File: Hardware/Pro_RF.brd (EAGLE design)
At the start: 40.6 x 27.9 mm, 102 parts, among them U1 MCP73831, U2 915MHz, U5 ATmega32U4, U6 3.3V, Y2 8MHz

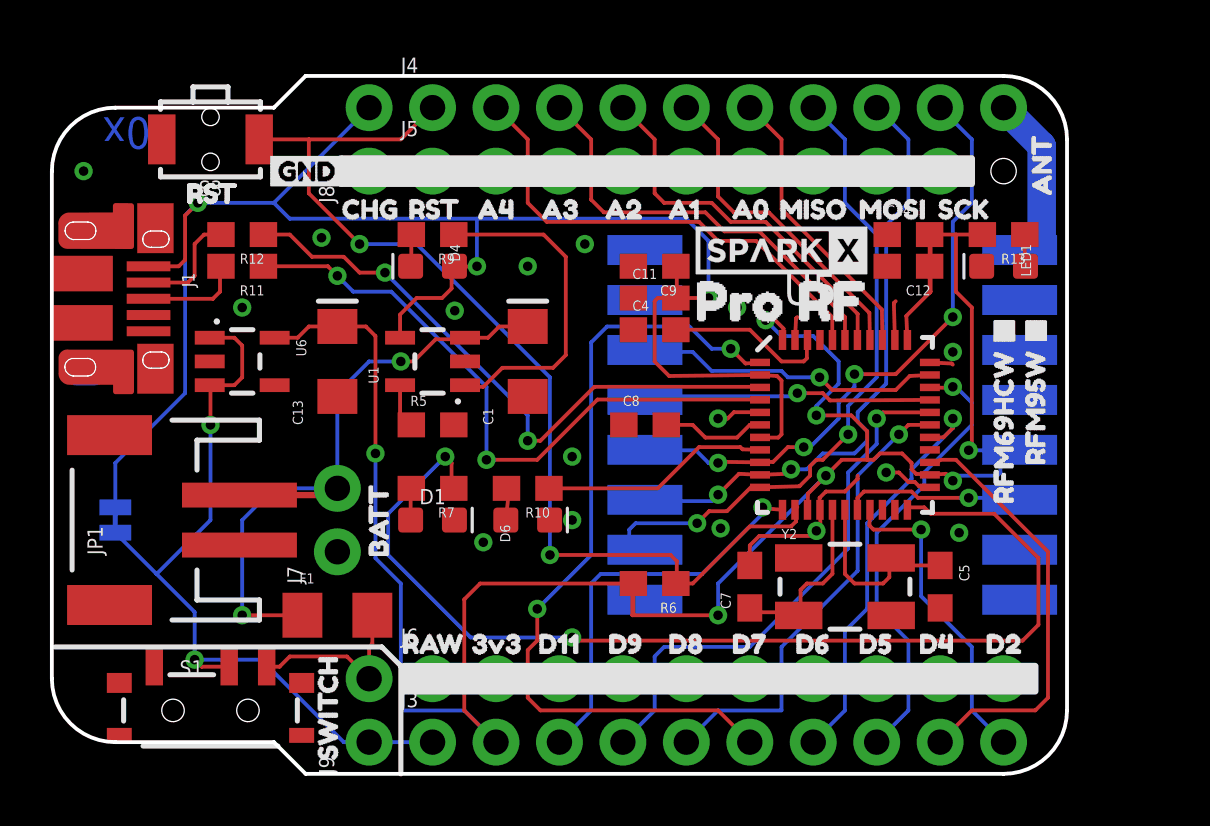
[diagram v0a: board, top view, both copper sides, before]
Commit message: Adding prod IDs. This changed some FPs so fixed routes. Moved Int Pin to avoid I2C
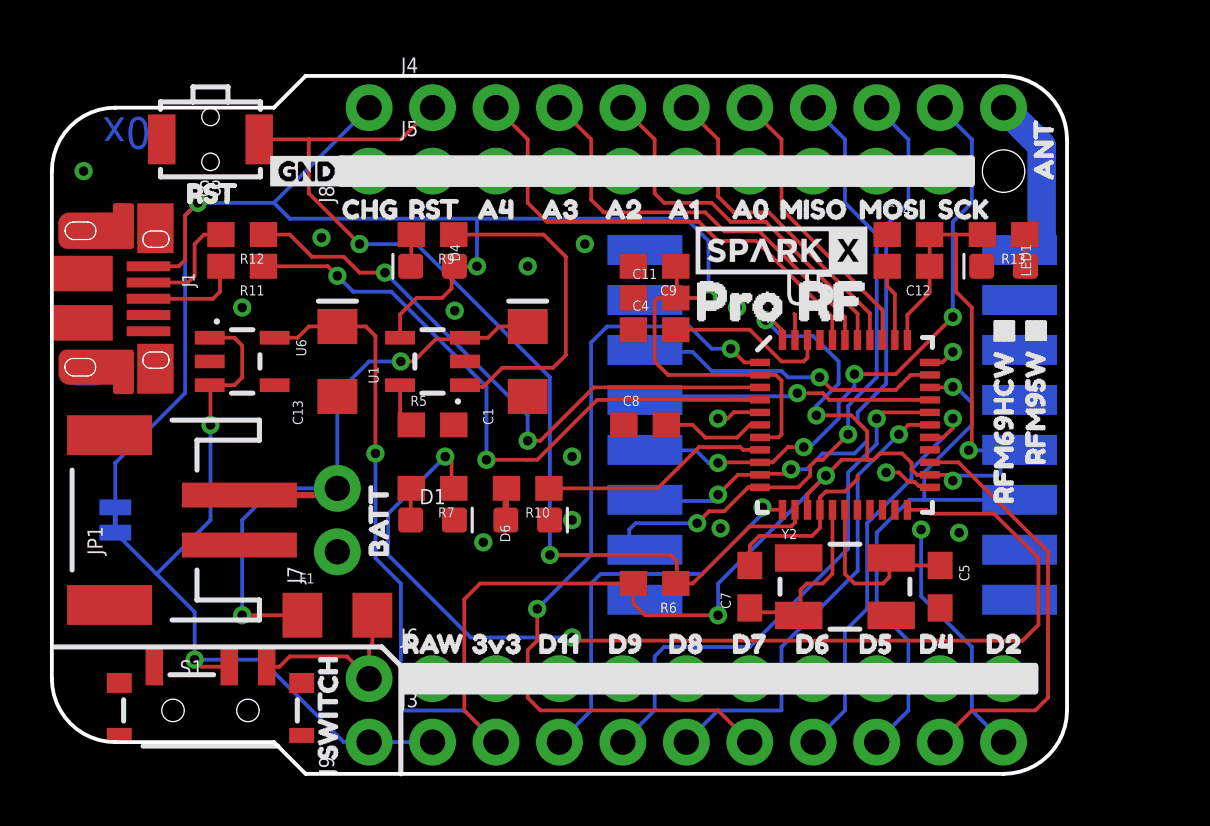
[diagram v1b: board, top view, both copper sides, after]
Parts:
- R10, R13, R7, R9: value 330 -> 1k
- S1: value (none) -> Power
- moved U$11 0.63 mm to (39.7, 23.1)
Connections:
- removed net D3: U2.14, U5.18
- removed net D5: J3.8, U5.31
- new net RFM_INT: J3.8, U2.14, U5.31
- new net SCL: U5.18
- new net SDA: U5.19
- net D2: no longer U5.19
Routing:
- net RFM_INT: track 0.00 -> 22.4 mm, vias 0 -> 1
- net D5: track 18.2 -> 0.00 mm, vias 1 -> 0
- net D3: track 7.21 -> 0.00 mm, vias 1 -> 0
- net 3.3V: track 92.5 -> 88.5 mm
- net D2: track 12.6 -> 9.88 mm
- net GND: track 14.6 -> 16.3 mm, vias 16 -> 15

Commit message: Many updates. v02.
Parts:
- removed U$61: (no value), buzzard_labels (25):D212
- removed U5: ATmega32U4, SparkFun-IC-Microcontroller:QFN-44-NOPAD
- added D2: BLUE, SparkFun-LED:LED-0603
- added J10: AVR_SPI_PROG_3X2TESTPOINTS, SparkFun-Connectors:2X3_TEST_POINTS
- added J11: (no value), SparkFun-Connectors:1X09_NO_SILK
- added J12: JST, SparkFun-Connectors:JST-2-SMD
- added J2: (no value), SparkFun-Connectors:1X04_1MM_RA
- added JP2: (no value), SparkFun-Jumpers:SMT-JUMPER_2_NO_SILK
- added R1, R2: 10k, SparkFun-Resistors:0603
- added R3: 1k, SparkFun-Resistors:0603
- added U$62: (no value), buzzard_labels (25):GND0
- added U$63: (no value), Labels:PWR-()-03
- added U$65: (no value), buzzard_labels (9):CHG1
- added U$66: (no value), Labels:QWIIC-()-04
- added U$68: (no value), buzzard_labels (9):D100
- added U$69: (no value), buzzard_labels (8):TX3
- added U$70: (no value), buzzard_labels (8):TX6
- added U$71: (no value), buzzard_labels (8):STAT5
- added U$72: (no value), buzzard_labels (8):RX7
- added U$73: (no value), buzzard_labels (8):RX2
- added U$74: (no value), buzzard_labels (25):D514
- added U3: 32U4, SparkFun-IC-Microcontroller:QFN-44-NOPAD
- D1: value GREEN -> Green
- D6: value BLUE -> Yellow
- J4: device SparkFun-Connectors:1X10_NO_SILK -> SparkFun-Connectors:1X01_NO_SILK
- J7: value (none) -> PTH
- J9: value (none) -> External On/Off
- JP1: device SparkFun-Connectors:JST-2-SMD -> SparkFun-Jumpers:SMT-JUMPER_2_NO_SILK
- SJ2: device SparkFun:SJ_2S-TRACE -> SparkFun-Jumpers:SMT-JUMPER_2_NC_TRACE_SILK
- U$15: device buzzard_labels (25):D212 -> buzzard_labels (10):D90
- U$16: device buzzard_labels (25):D413 -> buzzard_labels (10):D90
- U$17: device buzzard_labels (25):D514 -> buzzard_labels (25):GND0
- U$19: device buzzard_labels (25):D716 -> buzzard_labels (8):RX2
- U$21: device buzzard_labels (25):D918 -> buzzard_labels (9):D100
- U$25: device buzzard_labels (26):RFM69HCW_#0 -> buzzard_labels (3):LORA0
- U$26: value (none) -> SPECIAL_INSTRUCTIONS-ORDERING; device buzzard_labels (26):RFM95W_#1 -> SparkFun-Aesthetics:ORDERING_INSTRUCTIONS
- U$35: device buzzard_labels (25):RST2 -> buzzard_labels (3):WAN1
- U$55: device buzzard_labels (25):D918 -> buzzard_labels (25):D514
- U$57: device buzzard_labels (25):D716 -> buzzard_labels (8):TX3
- U$59: device buzzard_labels (25):D514 -> buzzard_labels (12):RFM69HCW#1
- U$60: device buzzard_labels (25):D413 -> buzzard_labels (12):RFM95W#0
- moved U$26 78.0 mm to (-34.3, -14.0), turned to 0 degrees
- moved R13 26.7 mm to (11.4, 21.1)
- moved J4 23.0 mm to (38.1, 24.1)
- moved U$25 22.3 mm to (15.9, 11.7), flipped to the bottom, turned to 270 degrees
- moved U$60 19.4 mm to (19.7, 13.7)
- moved LED1 19.1 mm to (19.1, 21.1), turned to 0 degrees
- moved C14 18.1 mm to (22.9, 7.62), turned to 90 degrees
- moved U$35 17.0 mm to (17.1, 11.7), flipped to the bottom, turned to 270 degrees
- moved U$59 16.0 mm to (22.2, 15.5)
- moved JP1 15.2 mm to (19.1, 10.2), flipped to the bottom, turned to 180 degrees
- moved U$51 15.2 mm to (2.54, 24.1)
- moved U$1 14.1 mm to (32.3, 7.24)
- moved U$19 13.1 mm to (39.6, 5.21), flipped to the bottom
- moved R6 12.8 mm to (25.4, 20.3), turned to 270 degrees
- moved U$15 12.7 mm to (24.0, 5.21)
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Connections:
- removed net A5: U5.41
- removed net D14: R10.1, U5.8
- removed net D2: J3.10
- removed net D4: J3.9, U5.25
- removed net D7: J3.6, U5.1
- removed net N$15: D1.A, R7.2
- removed net N$19: D6.A, R10.2
- removed net RST: J4.1, R6.1, S3.1, U5.13
- new net !CS: U2.5, U3.41
- new net !RST: J10.5, J11.1, R6.1, S3.1, U3.13
- new net D5: J3.8, U3.31
- new net N$1: D6.C, R10.2
- new net N$2: D1.C, R7.2
- new net N$3: D2.A, R3.1
- new net RFM_IO1: JP1.1, U2.15
- new net RFM_IO2: JP2.1, U2.16
- new net RXLED: R10.1, U3.8
- new net SHLD: J1.SHIELD, J1.SHIELD10, J1.SHIELD2, J1.SHIELD3, J1.SHIELD4, J1.SHIELD5, J1.SHIELD6, J1.SHIELD7, J1.SHIELD8, J1.SHIELD9
- new net STAT: R3.2, U3.32
- net 3.3V: now also D1.A, D6.A, J10.2, J2.2, U3.14, U3.24, U3.34, U3.44; no longer U5.14, U5.24, U5.34, U5.44
- net A0: now also J11.6, U3.36; no longer J4.6, U5.36
- net A1: now also J11.5, U3.37; no longer J4.5, U5.37
- net A2: now also J11.4, U3.38; no longer J4.4, U5.38
- net A3: now also J11.3, U3.39; no longer J4.3, U5.39
- net A4: now also J11.2, U3.40; no longer J4.2, U5.40
- net ANT: now also J4.1; no longer J4.10
- net AREF: now also U3.42; no longer U5.42
- net D+: now also U3.4; no longer U5.4
- net D-: now also U3.3; no longer U5.3
- net D10: now also J3.4, JP1.2, U3.30; no longer U2.5, U5.30
- net D11: now also JP2.2, U3.12; no longer U5.12
- net D6: now also U3.27; no longer U5.27
- net D8: now also J3.6, U3.28; no longer J3.5, U5.28
- net D9: now also J3.5, U3.29; no longer J3.4, U5.29
- net GND: now also D2.C, J10.6, J12.1, J2.1, R2.1, U3.15, U3.23, U3.33, U3.35, U3.43, U3.5; no longer D1.C, D6.C, JP1.1, U5.15, U5.23, U5.33, U5.35, U5.43, U5.5
- net MISO: now also J10.1, J11.7, U3.11; no longer J4.7, U5.11
- net MOSI: now also J10.4, J11.8, U3.10; no longer J4.8, U5.10
- net N$16: now also U3.16; no longer U5.16
- net N$17: now also U3.17; no longer U5.17
- net RFM_INT: now also U3.1; no longer J3.8, U5.31
- net RFM_RST: now also U3.25; no longer U5.32
- net RXI: now also J3.10, U3.20; no longer U5.20
- net SCK: now also J10.3, J11.9, U3.9; no longer J4.9, U5.9
- net SCL: now also J2.4, U3.18; no longer U5.18
- net SDA: now also J2.3, U3.19; no longer U5.19
- net TXLED: now also U3.22; no longer U5.22
- net TXO: now also J3.9, U3.21; no longer U5.21
- net UCAP: now also U3.6; no longer U5.6
- net USB_VCC: now also U3.2, U3.7; no longer U5.2, U5.7
- net VBATT: now also J12.2, R1.2; no longer JP1.2
- net VBATT_LVL: now also R1.1, R2.2, U3.26; no longer U5.26
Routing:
- net RST: track 41.8 -> 0.00 mm, vias 2 -> 0
- net VBATT_LVL: track 0.00 -> 37.8 mm, vias 0 -> 4
- net !RST: track 0.00 -> 36.1 mm, vias 0 -> 1
- net RFM_IO1: track 0.00 -> 35.4 mm, vias 0 -> 2
- net D10: track 11.6 -> 44.6 mm, vias 1 -> 4
- net D7: track 32.5 -> 0.00 mm, vias 2 -> 0
- net RFM_IO2: track 0.00 -> 27.7 mm
- net TXLED: track 42.7 -> 15.5 mm
- net RFM_RST: track 12.3 -> 34.1 mm, vias 1 -> 3
- net D5: track 0.00 -> 19.7 mm, vias 0 -> 1
- net D4: track 17.1 -> 0.00 mm
- net SCL: track 0.00 -> 13.1 mm, vias 0 -> 2
- net 3.3V: track 88.5 -> 101.4 mm, vias 7 -> 8
- net SDA: track 0.00 -> 12.0 mm, vias 0 -> 2
- net RXI: track 0.00 -> 11.8 mm, vias 0 -> 1
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- added copper zone on layer 1, net SHLD
- added copper zone on layer 16, net SHLD
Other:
- board text added: "+"
- board text added: "-"
- board text added: "0.8mm Board Thickness"
- board text added: "x02"
- board text removed: "x01"

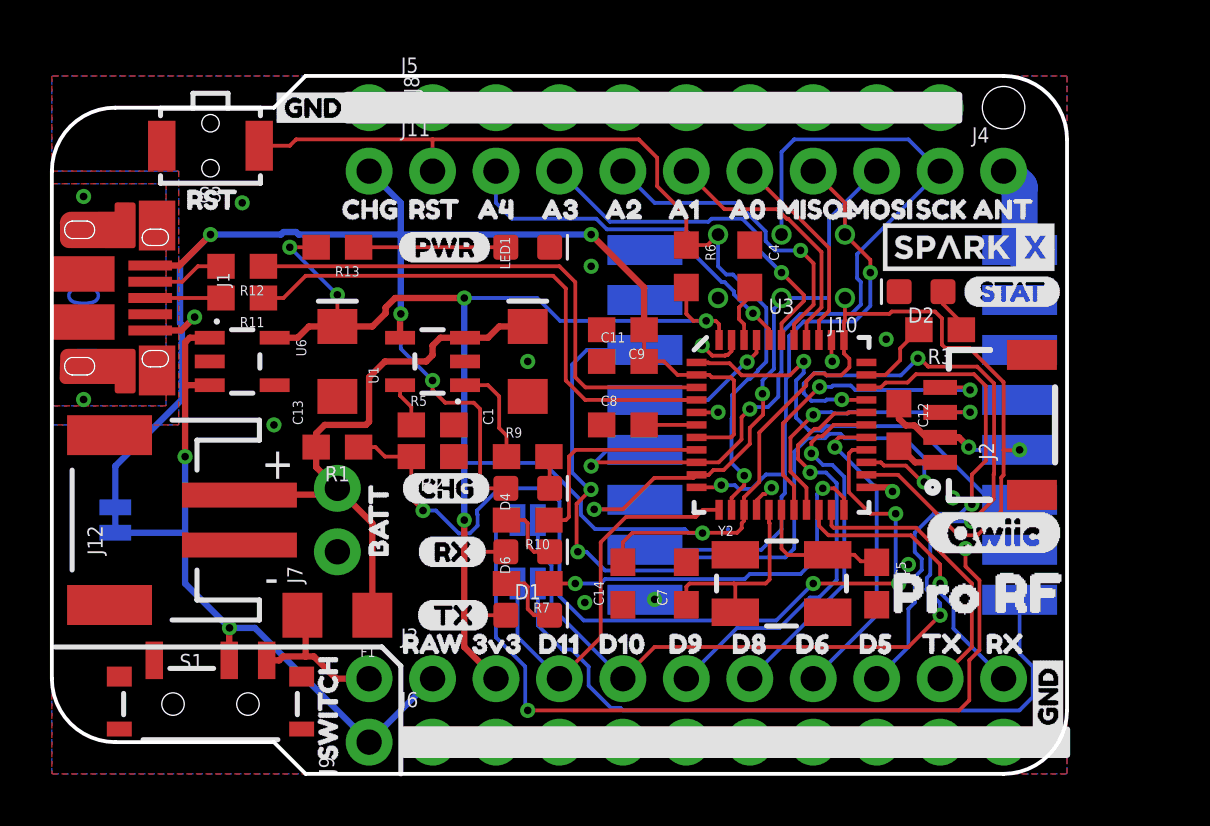
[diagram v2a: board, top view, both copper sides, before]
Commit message: Adding pullup to CS
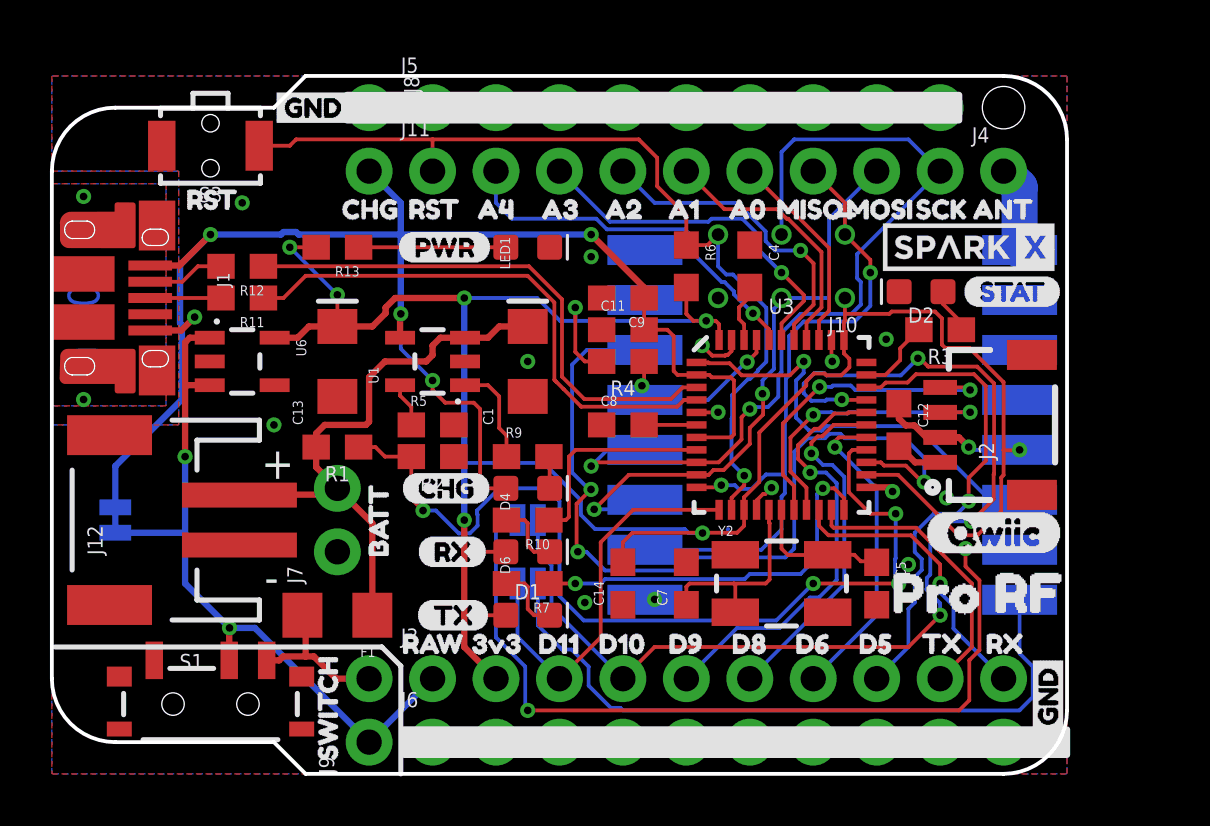
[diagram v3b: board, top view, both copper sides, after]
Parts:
- added R4: 10k, SparkFun-Resistors:0603
- moved C11 1.27 mm to (22.9, 17.8)
- moved C9 1.27 mm to (22.9, 19.1)
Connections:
- net !CS: now also R4.1
- net 3.3V: now also R4.2
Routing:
- net 3.3V: track 101.4 -> 104.9 mm, vias 8 -> 9
- net !CS: track 5.76 -> 7.39 mm, vias 1 -> 2

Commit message: Adding Examples
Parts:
- added FD1, FD2, FD3, FD4: FIDUCIAL1X2, SparkFun-Aesthetics:FIDUCIAL-1X2
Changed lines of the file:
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@@
 <attribute name="PROD_ID" value="RES-00824" x="22.86" y="16.51" size="1.778" layer="27" font="vector" ratio="15" rot="R180" display="off"/>
 </element>
+<element name="FD1" library="SparkFun-Aesthetics" package="FIDUCIAL-1X2" value="FIDUCIAL1X2" x="1.27" y="2.54" rot="MR0"/>
+<element name="FD2" library="SparkFun-Aesthetics" package="FIDUCIAL-1X2" value="FIDUCIAL1X2" x="39.37" y="25.4" rot="MR0"/>
+<element name="FD3" library="SparkFun-Aesthetics" package="FIDUCIAL-1X2" value="FIDUCIAL1X2" x="1.27" y="2.54"/>
+<element name="FD4" library="SparkFun-Aesthetics" package="FIDUCIAL-1X2" value="FIDUCIAL1X2" x="39.37" y="25.4"/>
 </elements>
 <signals>
@@
 <wire x1="25.03565625" y1="14.6986" x2="25.30705625" y2="14.97" width="0.1524" layer="1"/>
 <wire x1="21.19234375" y1="14.6986" x2="25.03565625" y2="14.6986" width="0.1524" layer="1"/>
-<wire x1="21.19234375" y1="14.6986" x2="20.485471875" y2="15.405471875" width="0.1524" layer="1"/>
-<wire x1="20.485471875" y1="15.405471875" x2="20.193" y2="15.69794375" width="0.1524" layer="1"/>
+<wire x1="21.19234375" y1="14.6986" x2="20.1168" y2="15.77414375" width="0.1524" layer="1"/>
 <wire x1="20.1168" y1="18.8722" x2="19.05" y2="19.939" width="0.1524" layer="1"/>
-<wire x1="20.193" y1="15.69794375" x2="20.1168" y2="15.77414375" width="0.1524" layer="1"/>
 <wire x1="20.1168" y1="15.77414375" x2="20.1168" y2="18.8722" width="0.1524" layer="1"/>
 </signal>
@@
 <wire x1="31.75" y1="18.1356" x2="31.71" y2="18.0956" width="0.1524" layer="1"/>
 <wire x1="33.528" y1="18.415" x2="31.75" y2="18.415" width="0.1524" layer="1"/>
-<wire x1="33.877" y1="11.97" x2="35.6235" y2="10.2235" width="0.1524" layer="1"/>
-<wire x1="35.6235" y1="10.2235" x2="36.2966" y2="9.5504" width="0.1524" layer="1"/>
+<wire x1="33.877" y1="11.97" x2="36.2966" y2="9.5504" width="0.1524" layer="1"/>
 <wire x1="30.51305625" y1="16.0274" x2="30.2006" y2="15.71494375" width="0.1524" layer="1"/>
 <wire x1="30.2006" y1="15.71494375" x2="30.2006" y2="15.54554375" width="0.1524" layer="1"/>

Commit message: updating to sparkfun silk
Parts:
- removed U$2, U$30: (no value), SparkX:SPARKX-SMALL
- added LOGO1: REVISION, SparkFun-Aesthetics:REVISION
- added LOGO2: SFE_LOGO_NAME.1_INCH, SparkFun-Aesthetics:SFE_LOGO_NAME_.1
- added LOGO3: SFE_LOGO_NAME_FLAME.1_INCH, SparkFun-Aesthetics:SFE_LOGO_NAME_FLAME_.1
- moved U$31 4.27 mm to (22.5, 16.4)
- moved U$26 2.54 mm to (-34.3, -16.5)
- moved U$59 0.76 mm to (22.2, 14.7)
- moved U$60 0.51 mm to (19.7, 13.2)
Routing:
- net !CS: track 7.39 -> 10.7 mm
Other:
- board text added: "Andy England"
- board text added: "Elias Santistevan"

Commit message: Clean up
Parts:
- added J13: U.FL, SparkFun-Connectors:U.FL
- moved LOGO2 18.5 mm to (44.8, 9.27), turned to 90 degrees
- moved U$71 4.82 mm to (31.9, 20.8)
- moved D2 0.80 mm to (34.0, 19.6)
- moved C9 0.51 mm to (22.9, 19.6)
- moved R2 0.25 mm to (15.2, 12.4)
- moved C11 0.25 mm to (22.9, 18.0)
- moved R11 0.13 mm to (7.62, 18.9)
- moved LED1 0.13 mm to (19.1, 21.2)
- moved R12 0.13 mm to (7.62, 20.4)
- moved R13 0.13 mm to (11.4, 21.2)
- moved U$63 0.13 mm to (13.8, 21.2)
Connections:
- net ANT: now also J13.FEED
- net GND: now also J13.1, J13.2
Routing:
- net ANT: track 3.43 -> 6.14 mm
- net 3.3V: track 104.8 -> 103.2 mm
- net SHLD: track 0.21 -> 1.21 mm
- net TXLED: track 15.5 -> 14.6 mm
- net D6: track 12.6 -> 11.7 mm
- net N$6: track 8.15 -> 7.45 mm
- net N$3: track 1.85 -> 2.43 mm
- net MOSI: track 23.7 -> 23.2 mm
